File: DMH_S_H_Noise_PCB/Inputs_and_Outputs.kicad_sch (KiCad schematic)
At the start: 0 parts

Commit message: Finished schematic
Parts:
- added J1, J2, J3, J4, J5, J6, J7, J8: TS_Jack_6.35mm_Sw, SynthStuff:CUI_MJ-63052A, symbol SynthStuff:TS_Jack_6.35mm_Sw
- added J200: IDC_02x05, SynthStuff:IDC-Header_2x05_P2.54mm_Vertical_BackBone, symbol SynthStuff:BackBone_Connector_10Pin
- added J50, J60, J70: Conn_01x05, Connector_PinHeader_2.54mm:PinHeader_1x05_P2.54mm_Vertical, symbol Connector_Generic:Conn_01x06
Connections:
- new net: J200.1 (Pin_1), J4.TN, J70.1 (Pin_1)
- new net: J200.2 (Pin_2), J5.TN, J70.2 (Pin_2)
- new net: J200.3 (Pin_3), J6.TN, J70.3 (Pin_3)
- new net: J200.4 (Pin_4), J7.TN, J70.4 (Pin_4)
- new net: J200.5 (Pin_5), J70.5 (Pin_5), J8.TN
- new net Blue: J60.5 (Pin_5), J8.T
- new net External Clock: J3.T, J50.4 (Pin_4)
- new net GND: J1.S, J2.S, J200.10 (Pin_10), J200.6 (Pin_6), J200.7 (Pin_7), J200.8 (Pin_8), J200.9 (Pin_9), J3.S, J4.S, J5.S, J50.6 (Pin_6), J6.S, J60.6 (Pin_6), J7.S, J70.6 (Pin_6), J8.S
- new net Input: J1.T, J50.1 (Pin_1)
- new net Internal Clock: J3.TN, J50.5 (Pin_5)
- new net Pink: J6.T, J60.3 (Pin_3)
- new net S&H: J2.TN, J50.3 (Pin_3)
- new net S&H Out: J4.T, J60.1 (Pin_1)
- new net Slew In: J2.T, J50.2 (Pin_2)
- new net Slew Out: J5.T, J60.2 (Pin_2)
- new net White: J1.TN, J60.4 (Pin_4), J7.T

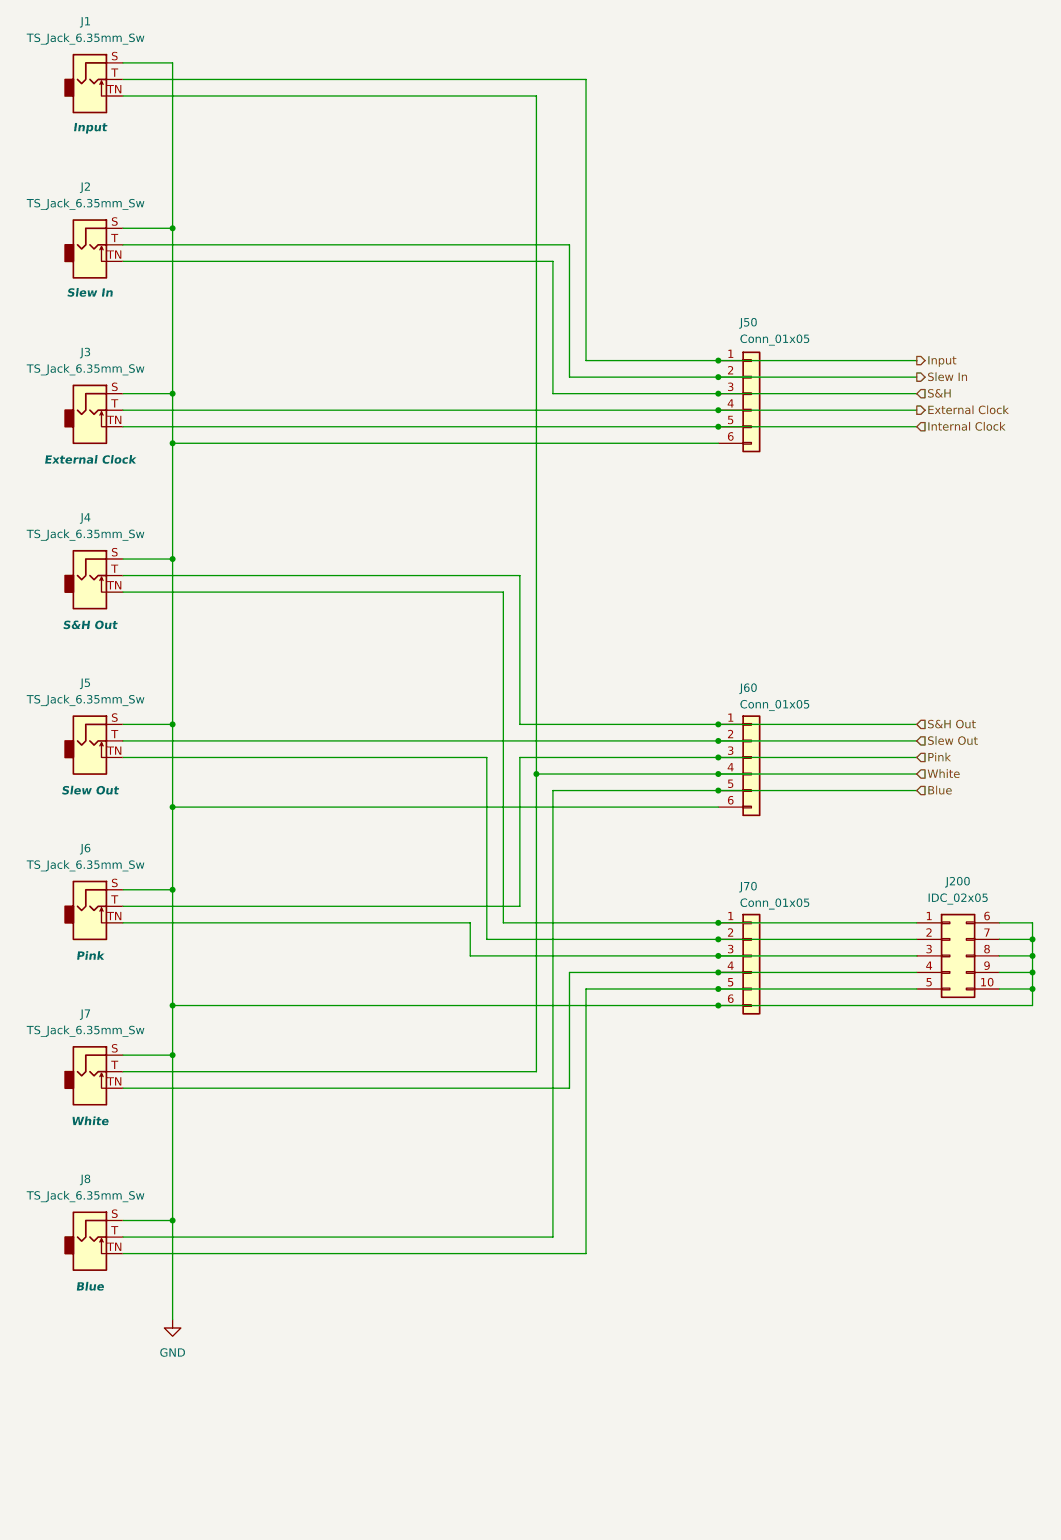
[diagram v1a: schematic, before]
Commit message: Added clock output
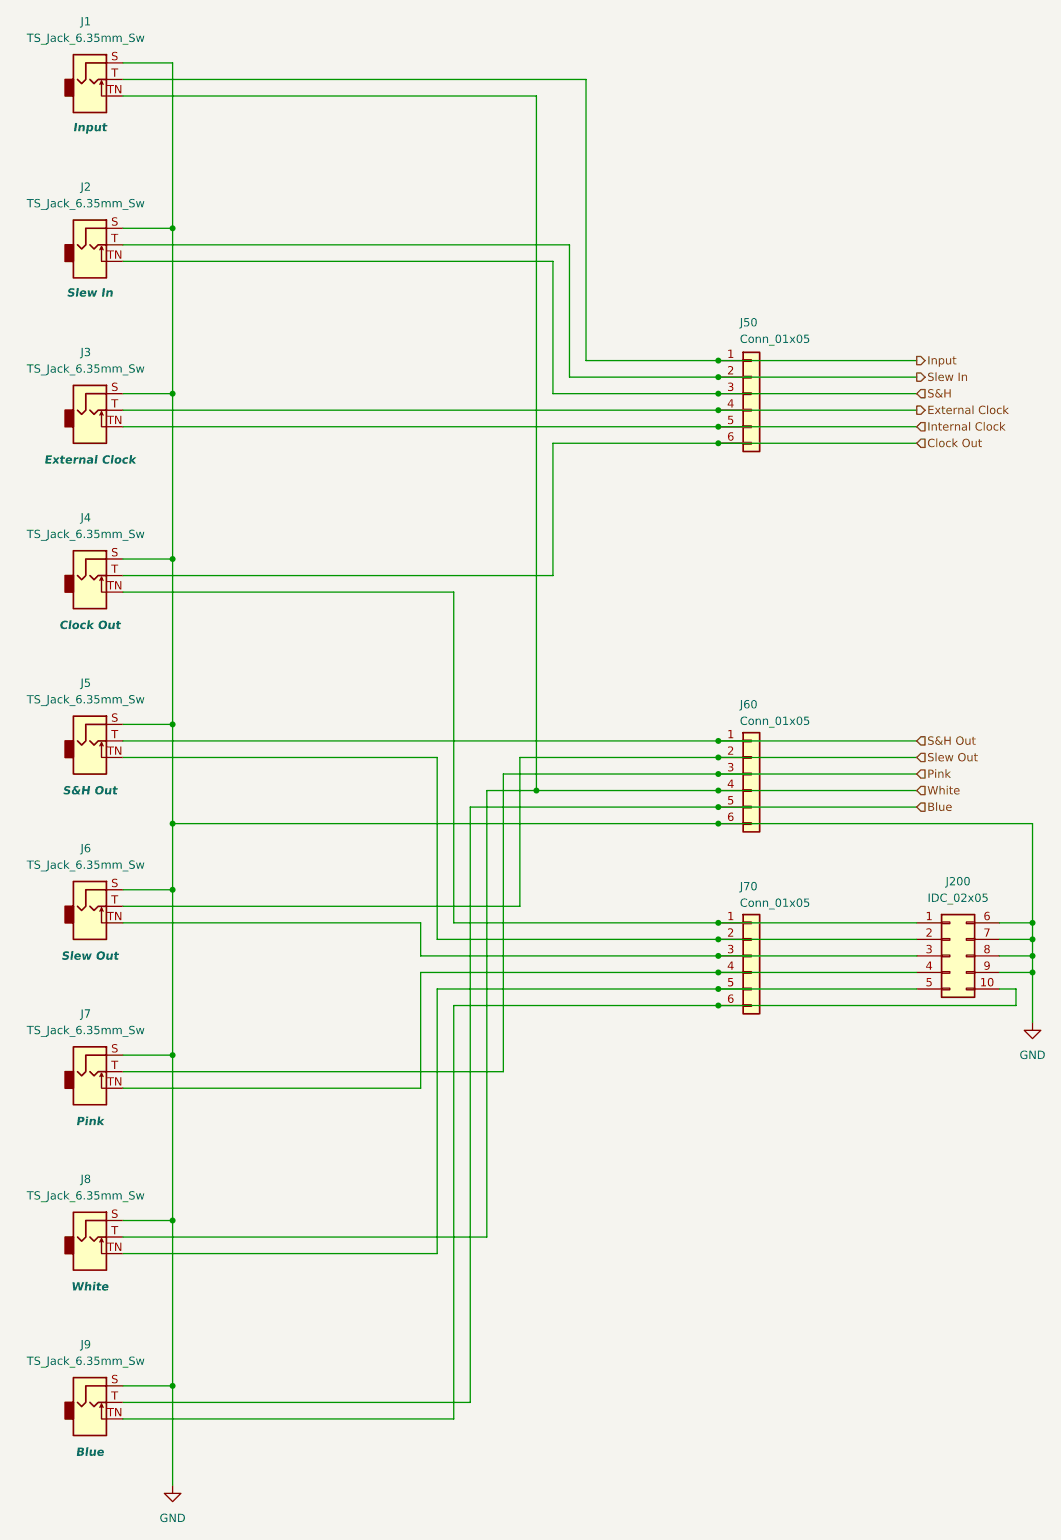
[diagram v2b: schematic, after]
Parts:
- added J9: TS_Jack_6.35mm_Sw, SynthStuff:CUI_MJ-63052A, symbol SynthStuff:TS_Jack_6.35mm_Sw
- J4: Function S&H Out -> Clock Out
- J5: Function Slew Out -> S&H Out
- J6: Function Pink -> Slew Out
- J7: Function White -> Pink
- J8: Function Blue -> White
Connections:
- net Blue: now also J9.T; no longer J8.T
- net GND: now also J9.S; no longer J200.10 (Pin_10), J50.6 (Pin_6), J70.6 (Pin_6)
- net Pink: now also J7.T; no longer J6.T
- net S&H Out: now also J5.T; no longer J4.T
- net Slew Out: now also J6.T; no longer J5.T
- net White: now also J8.T; no longer J7.T
- new net: J200.10 (Pin_10), J70.6 (Pin_6), J9.TN
- new net Clock Out: J4.T, J50.6 (Pin_6)
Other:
- moved on the sheet: J60

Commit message: Component placement ongoing
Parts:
- J50, J60, J70: value Conn_01x05 -> Conn_01x06; footprint Connector_PinHeader_2.54mm:PinHeader_1x05_P2.54mm_Vertical -> Connector_PinHeader_2.54mm:PinHeader_1x06_P2.54mm_Vertical
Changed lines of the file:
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@@
 			)
 		)
-		(property "Value" "Conn_01x05"
+		(property "Value" "Conn_01x06"
 			(at 137.922 164.592 0)
 			(effects
@@
 			)
 		)
-		(property "Footprint" "Connector_PinHeader_2.54mm:PinHeader_1x05_P2.54mm_Vertical"
+		(property "Footprint" "Connector_PinHeader_2.54mm:PinHeader_1x06_P2.54mm_Vertical"
 			(at 139.7 172.72 0)
 			(effects
@@
 				)
 				(hide yes)
+			)
+		)
+		(property "Function" ""
+			(at 139.7 172.72 0)
+			(effects
+				(font
+					(size 1.27 1.27)
+				)
 			)
 		)
@@
 			)
 		)
-		(property "Value" "Conn_01x05"
+		(property "Value" "Conn_01x06"
 			(at 137.922 136.652 0)
 			(effects
@@
 			)
 		)
-		(property "Footprint" "Connector_PinHeader_2.54mm:PinHeader_1x05_P2.54mm_Vertical"
+		(property "Footprint" "Connector_PinHeader_2.54mm:PinHeader_1x06_P2.54mm_Vertical"
 			(at 139.7 144.78 0)
 			(effects
@@
 				)
 				(hide yes)
+			)
+		)
+		(property "Function" ""
+			(at 139.7 144.78 0)
+			(effects
+				(font
+					(size 1.27 1.27)
+				)
 			)
 		)
@@
 			)
 		)
-		(property "Value" "Conn_01x05"
+		(property "Value" "Conn_01x06"
 			(at 137.922 77.978 0)
 			(effects
@@
 			)
 		)
-		(property "Footprint" "Connector_PinHeader_2.54mm:PinHeader_1x05_P2.54mm_Vertical"
+		(property "Footprint" "Connector_PinHeader_2.54mm:PinHeader_1x06_P2.54mm_Vertical"
 			(at 139.7 86.36 0)
 			(effects
@@
 			)
 		)
+		(property "Function" ""
+			(at 139.7 86.36 0)
+			(effects
+				(font
+					(size 1.27 1.27)
+				)
+			)
+		)

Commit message: Finished connectors PCB
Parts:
- J50, J60, J70: footprint Connector_PinHeader_2.54mm:PinHeader_1x06_P2.54mm_Vertical -> Connector_PinSocket_2.54mm:PinSocket_1x06_P2.54mm_Vertical
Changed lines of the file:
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@@
 			)
 		)
-		(property "Footprint" "Connector_PinHeader_2.54mm:PinHeader_1x06_P2.54mm_Vertical"
+		(property "Footprint" "Connector_PinSocket_2.54mm:PinSocket_1x06_P2.54mm_Vertical"
 			(at 139.7 172.72 0)
 			(effects
@@
 			)
 		)
-		(property "Footprint" "Connector_PinHeader_2.54mm:PinHeader_1x06_P2.54mm_Vertical"
+		(property "Footprint" "Connector_PinSocket_2.54mm:PinSocket_1x06_P2.54mm_Vertical"
 			(at 139.7 144.78 0)
 			(effects
@@
 			)
 		)
-		(property "Footprint" "Connector_PinHeader_2.54mm:PinHeader_1x06_P2.54mm_Vertical"
+		(property "Footprint" "Connector_PinSocket_2.54mm:PinSocket_1x06_P2.54mm_Vertical"
 			(at 139.7 86.36 0)
 			(effects
